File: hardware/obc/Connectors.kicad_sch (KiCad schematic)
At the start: 20 parts, among them J301 USB_C_Receptacle_USB2.0, J302 Conn_High-Rel_4S2P, J303 Conn_01x06, J304 Conn_High-Rel_6P, J305 Conn_01x05, U301 Mem_MT29F4G01ABAFDWB, U302 Mem_MT29F4G01ABAFDWB

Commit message: obc: begun formal layout
Organized the components of the first two schematic pages into formal layout and switched out connector components. Introduced step files for previously developed footprints.
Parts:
- J303: footprint Connector_PinHeader_2.54mm:PinHeader_1x06_P2.54mm_Vertical -> Connector_PinHeader_2.54mm:PinHeader_1x06_P2.54mm_Horizontal
- J304: footprint SSE_Footprints:Harwin_M300-MV30645M1_6P_P3.0mm_Vertical -> SSE_Footprints:MMCX-6_UMPT-06-01-L-RA-WT-TR_P2.0mm
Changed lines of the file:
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@@
 			)
 		)
-		(property "Footprint" "Connector_PinHeader_2.54mm:PinHeader_1x06_P2.54mm_Vertical"
+		(property "Footprint" "Connector_PinHeader_2.54mm:PinHeader_1x06_P2.54mm_Horizontal"
 			(at 180.34 128.27 0)
 			(effects
@@
 			)
 		)
-		(property "Footprint" "SSE_Footprints:Harwin_M300-MV30645M1_6P_P3.0mm_Vertical"
+		(property "Footprint" "SSE_Footprints:MMCX-6_UMPT-06-01-L-RA-WT-TR_P2.0mm"
 			(at 185.42 80.01 0)
 			(effects
@@
 			)
 		)
-		(property "Datasheet" "https://cdn.harwin.com/pdfs/G125-MH1XXM4-XXAD000P.pdf"
+		(property "Datasheet" "https://content.harwin.com/m/89c5f84cda5e98a6/original/DRG-00577-Technical-Drawing-Datasheet-M300-MV30645M1-pdf.pdf"
 			(at 185.42 80.01 0)
 			(effects

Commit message: obc: design review 5/28 implemented
Entered step models, adjusted pin clearances, and edited footprints.
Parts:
- J304: Manufacturer_Name Harwin -> Samtec Inc.; Manufacturer_Part_Number M300-MV30645M1 -> UMPT-06-01-L-RA-WT-TR
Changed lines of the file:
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@@
 			)
 		)
-		(property "Datasheet" "https://content.harwin.com/m/89c5f84cda5e98a6/original/DRG-00577-Technical-Drawing-Datasheet-M300-MV30645M1-pdf.pdf"
+		(property "Datasheet" "https://suddendocs.samtec.com/productspecs/umpx.pdf?_gl=1*19esy1c*_ga*MTEwMjE5MzYzMy4xNzE3MDIxOTU2*_ga_3KFNZC07WW*MTcxNzAyMTk1Ni4xLjAuMTcxNzAyMTk1Ni42MC4wLjA."
 			(at 185.42 80.01 0)
 			(effects
@@
 			)
 		)
-		(property "Manufacturer_Part_Number" "M300-MV30645M1"
+		(property "Manufacturer_Part_Number" "UMPT-06-01-L-RA-WT-TR"
 			(at 185.42 80.01 0)
 			(effects
@@
 			)
 		)
-		(property "Manufacturer_Name" "Harwin"
+		(property "Manufacturer_Name" "Samtec Inc."
 			(at 185.42 80.01 0)
 			(effects

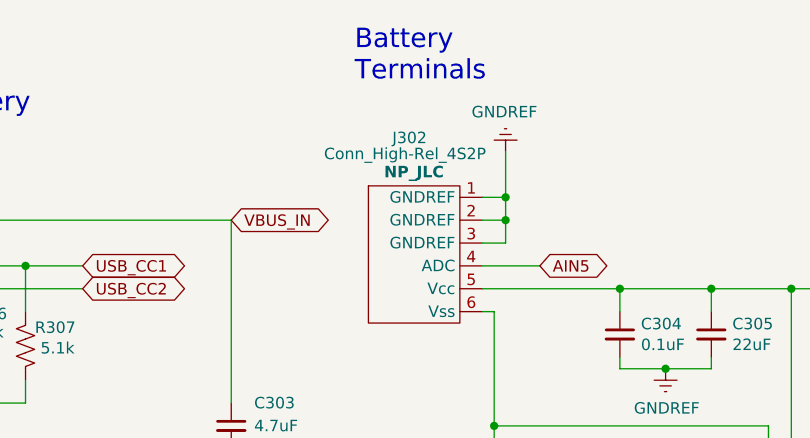
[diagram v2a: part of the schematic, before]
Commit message: obc: entered footprint and routed traces in a test subsection
Made harwin battery connector vertical and routed traces around U405 component.
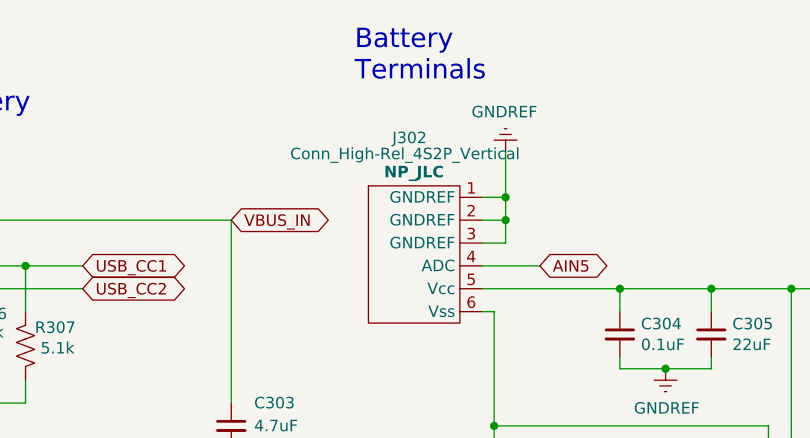
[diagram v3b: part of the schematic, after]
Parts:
- J302: value Conn_High-Rel_4S2P -> Conn_High-Rel_4S2P_Vertical; footprint SSE_Footprints:Harwin_G125-MH104M3-02AD000P_4S2P_P1.25mm_Horizontal -> SSE_Footprints:Harwin_G125-FV104F3-02AB000P_P1.25mm_Vertical; Manufacturer_Part_Number G125-MH104M3-02AD000P -> G125-FV104F3-02AB000P
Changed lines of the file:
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@@
 			)
 		)
-		(property "Value" "Conn_High-Rel_4S2P"
+		(property "Value" "Conn_High-Rel_4S2P_Vertical"
 			(at 151.384 38.354 0)
 			(effects
@@
 			)
 		)
-		(property "Footprint" "SSE_Footprints:Harwin_G125-MH104M3-02AD000P_4S2P_P1.25mm_Horizontal"
+		(property "Footprint" "SSE_Footprints:Harwin_G125-FV104F3-02AB000P_P1.25mm_Vertical"
 			(at 154.94 40.64 0)
 			(effects
@@
 			)
 		)
-		(property "Datasheet" "https://cdn.harwin.com/pdfs/G125-MH1XXM4-XXAD000P.pdf"
+		(property "Datasheet" "https://content.harwin.com/m/d362e7884ec41c62/original/DRG-03148-Technical-Drawing-Datasheet-G125-FV1XXF3-XXAB000P-pdf.pdf"
 			(at 154.94 40.64 0)
 			(effects
@@
 			)
 		)
-		(property "Manufacturer_Part_Number" "G125-MH104M3-02AD000P"
+		(property "Manufacturer_Part_Number" "G125-FV104F3-02AB000P"
 			(at 154.94 48.26 0)
 			(effects

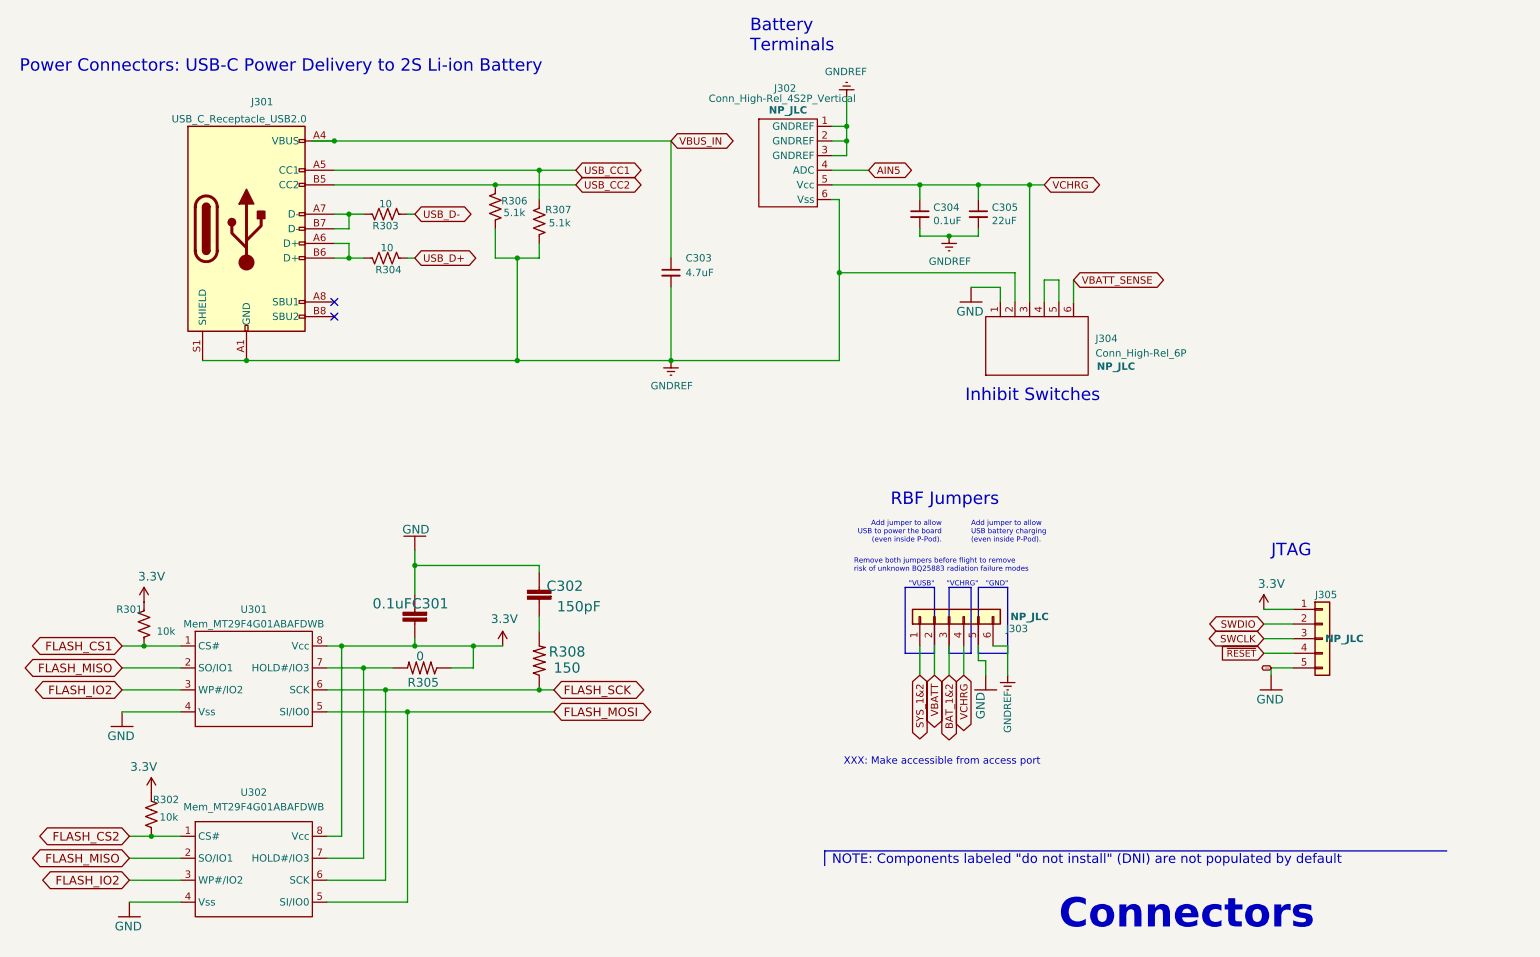
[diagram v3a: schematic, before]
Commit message: obc: power connection cleanup
Decreased track length to vias and centered all vias in pad. Updated schematic title blocks, edited 3D models.
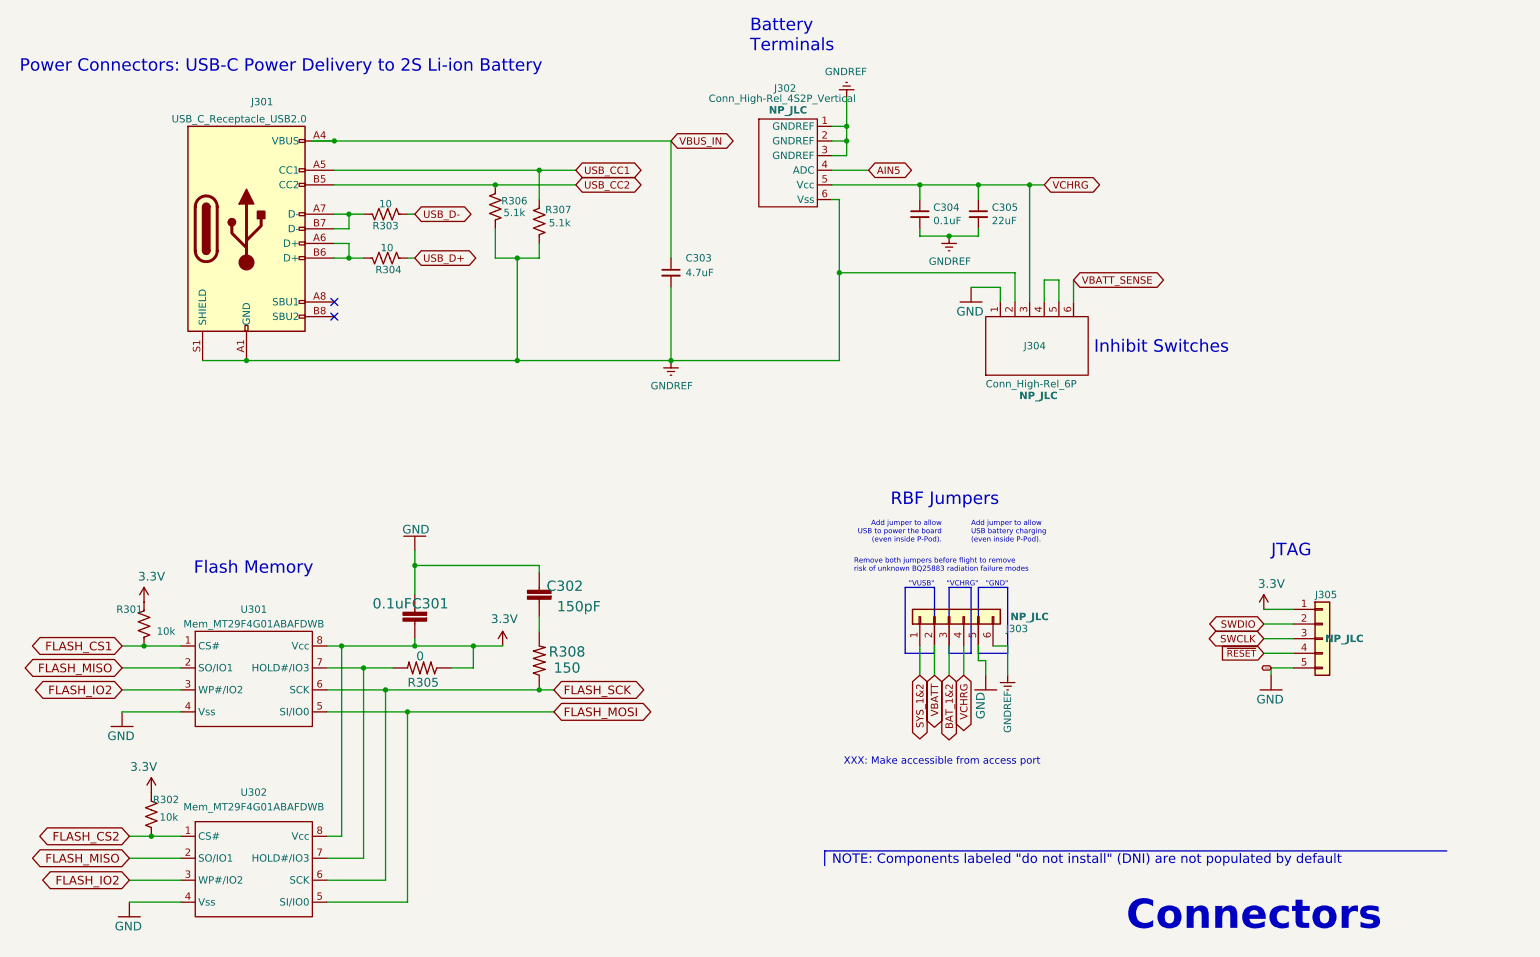
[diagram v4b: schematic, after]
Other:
- note added: "Flash Memory"
- company: Max Holliday -> Ruchir Kavulli, Michael Lyle
- title: PyCubed Mainboard -> Obi Wan Komputer
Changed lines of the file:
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@@
 	(paper "USLetter")
 	(title_block
-		(title "PyCubed Mainboard")
-		(date "2021-06-09")
-		(rev "v05c")
-		(company "Max Holliday")
+		(title "Obi Wan Komputer")
+		(date "2024-06-07")
+		(rev "vA")
+		(company "Ruchir Kavulli, Michael Lyle")
+		(comment 1 "Derived from PyCubed Mainboard v5")
 	)
 	(junction
@@
 	(text "Connectors"
 		(exclude_from_sim no)
-		(at 199.39 182.88 0)
+		(at 211.074 183.134 0)
 		(effects
 			(font
@@
 		)
 	)
+	(text "Flash Memory"
+		(exclude_from_sim no)
+		(at 49.276 121.158 0)
+		(effects
+			(font
+				(size 2.159 2.159)
+			)
+			(justify left bottom)
+		)
+	)
 	(text "Battery\nTerminals"
 		(exclude_from_sim no)
@@
 	(text "Inhibit Switches"
 		(exclude_from_sim no)
-		(at 183.134 91.186 0)
+		(at 205.486 82.804 0)
 		(effects
 			(font
@@
 		(dnp no)
 		(property "Reference" "J304"
-			(at 205.74 80.0099 90)
+			(at 193.294 81.28 90)
 			(effects
 				(font
@@
 		)
 		(property "Value" "Conn_High-Rel_6P"
-			(at 205.74 82.5499 90)
+			(at 186.69 87.884 90)
 			(effects
 				(font
@@
 		)
 		(property "DNI" "NP_JLC"
-			(at 209.296 84.836 90)
+			(at 195.834 89.916 90)
 			(effects
 				(font

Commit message: obc: test traces for high priority signals
Preliminary trace creation for high priority signals.
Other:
- title: Obi Wan Komputer -> Obi Wan Computer
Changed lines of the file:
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@@
 	(paper "USLetter")
 	(title_block
-		(title "Obi Wan Komputer")
+		(title "Obi Wan Computer")
 		(date "2024-06-07")
 		(rev "vA")

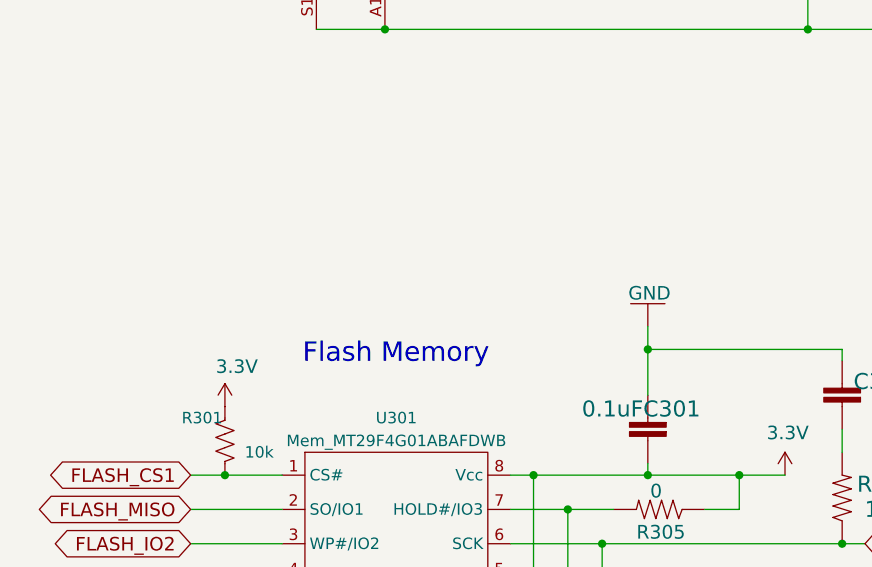
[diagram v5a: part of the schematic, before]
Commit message: obc: more preliminary routing
Still exploring problem space regarding routing, ~100 routed nets added.
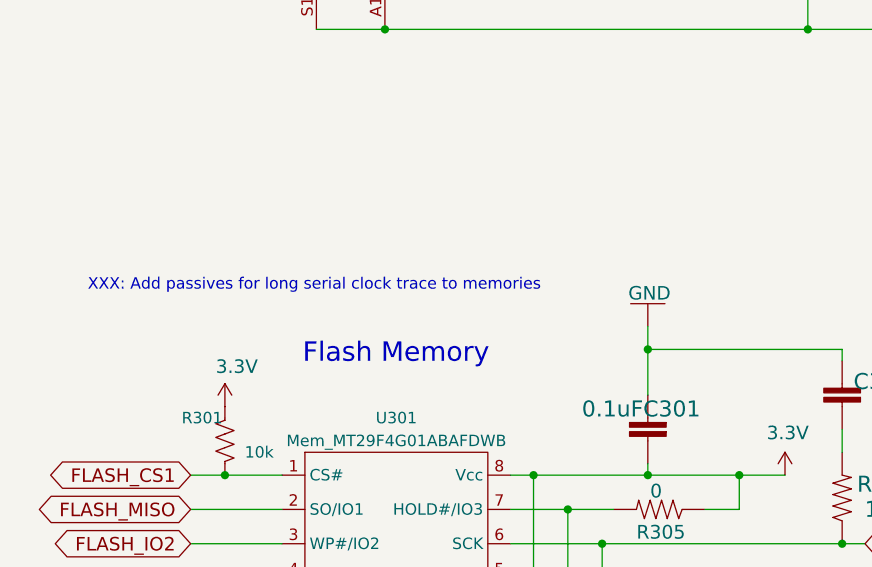
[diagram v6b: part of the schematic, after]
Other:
- note added: "XXX: Add passives for long serial clock trace to memories"
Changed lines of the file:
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@@
+		)
+	)
+	(text "XXX: Add passives for long serial clock trace to memories"
+		(exclude_from_sim no)
+		(at 25.4 113.03 0)
+		(effects
+			(font
+				(size 1.27 1.27)
+			)
+			(justify left bottom)
 		)
 	)
